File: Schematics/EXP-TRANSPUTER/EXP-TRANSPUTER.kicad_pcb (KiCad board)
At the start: 4 copper layers, 172 x 60 mm, 36 parts, among them IC2 74HCT373DW, IC5 CY62256N, J1 DIN41612_03x32_ABC_Male_Hor, J10 Conn_02x02_Odd_Even, J3 Conn_01x08, J4 Conn_01x08, J5 Conn_01x08, J6 Conn_01x08, J7 Conn_02x02_Odd_Even, J8 Conn_02x02_Odd_Even, J9 Conn_02x02_Odd_Even, U11 IMSC011, U2 ATF1502AS, U7 SN74LVC245APW

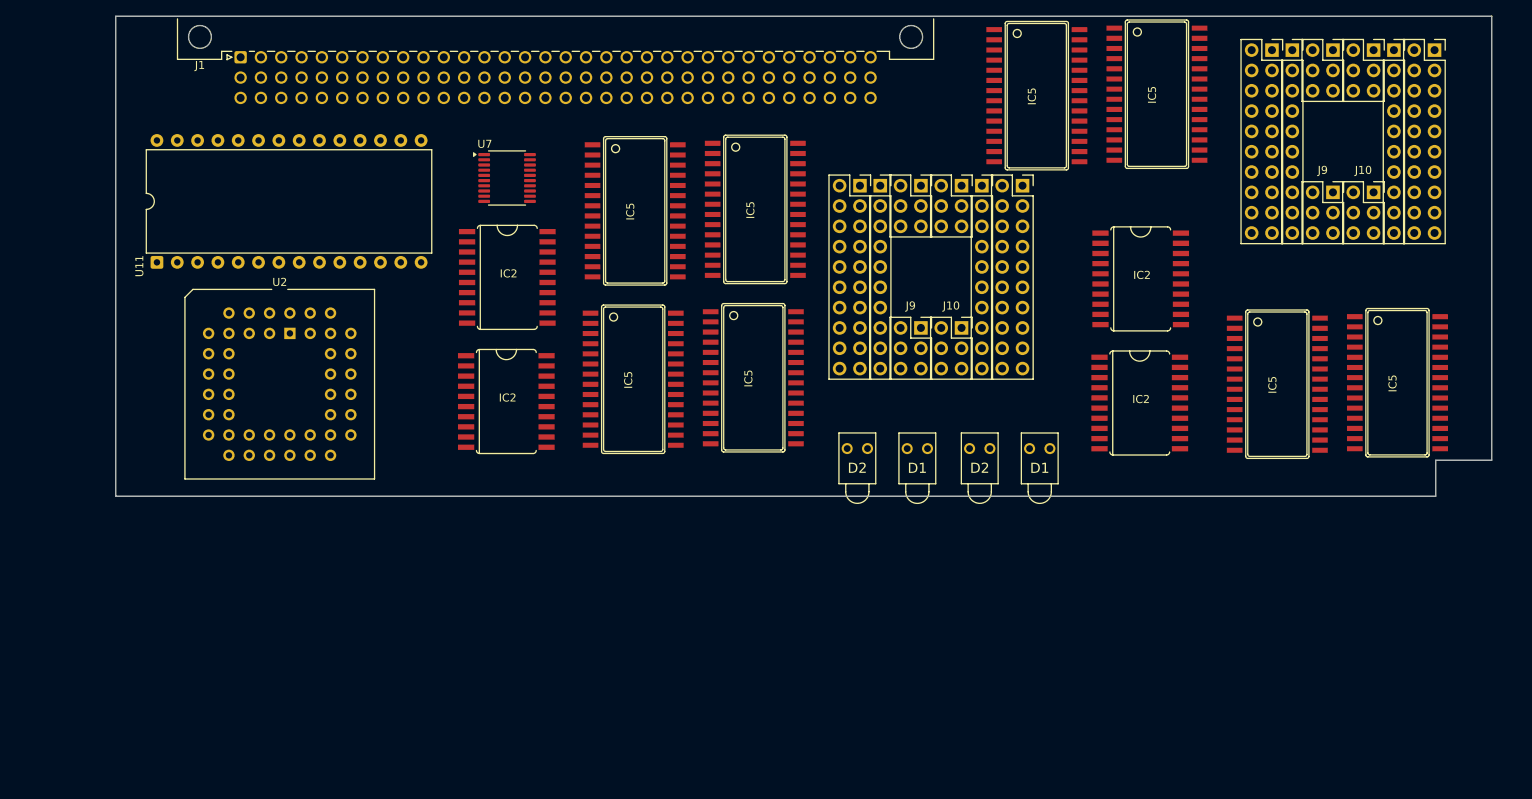
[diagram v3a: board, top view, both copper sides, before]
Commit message: Begun work on transputer expansion board
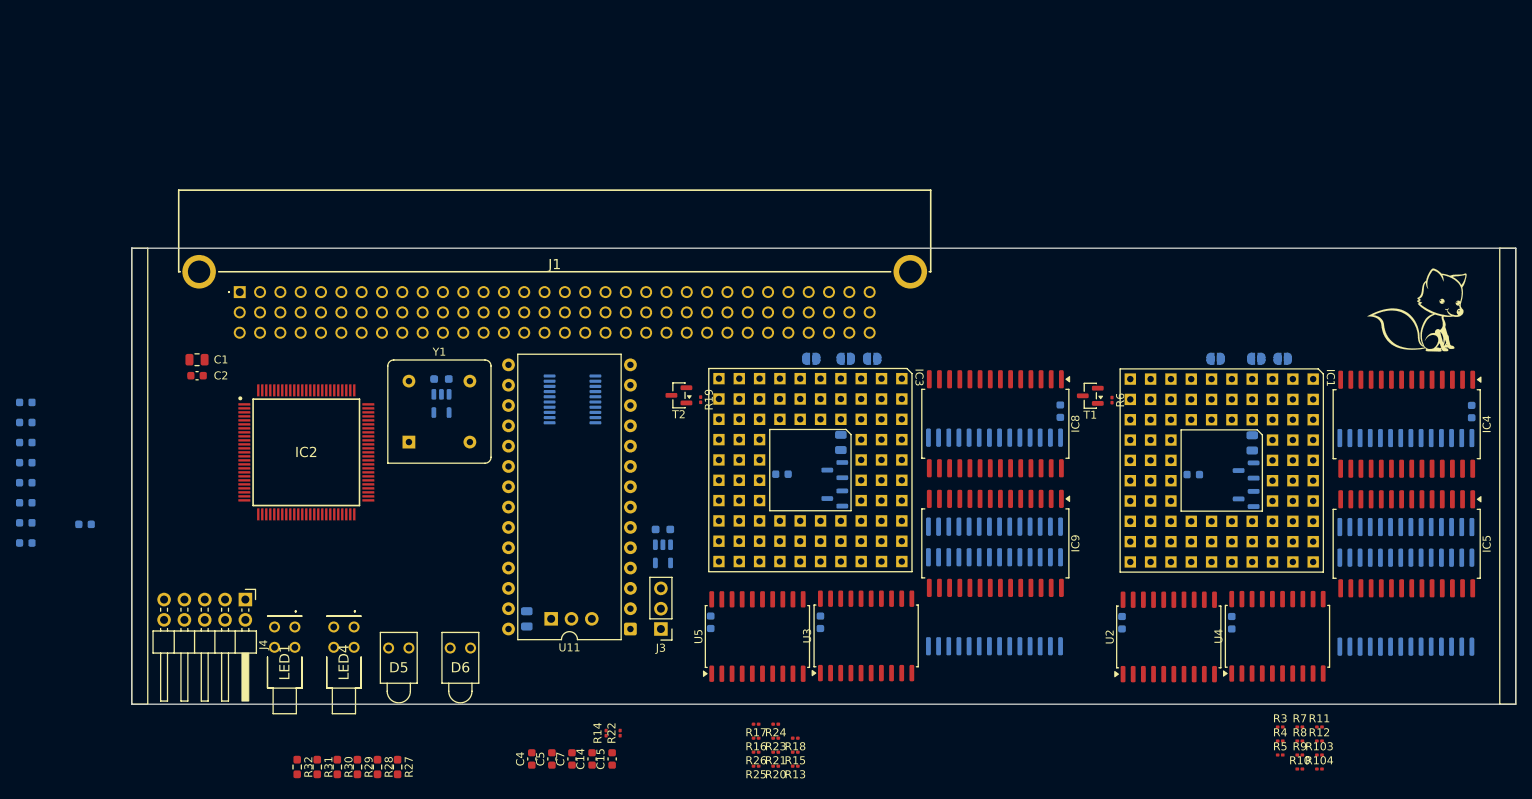
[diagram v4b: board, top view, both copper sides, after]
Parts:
- removed the D1 at (182.2, 95.0)
- removed the D1 at (166.9, 95.0)
- removed the D2 at (174.7, 95.0)
- removed the D2 at (159.4, 95.0)
- removed the IC2 at (116.9, 73.6)
- removed the IC2 at (116.8, 89.2)
- removed the IC2 at (196.0, 89.3)
- removed the IC2 at (196.1, 73.8)
- removed the IC5 at (183.1, 50.9)
- removed the IC5 at (132.9, 65.3)
- removed the IC5 at (198.2, 50.8)
- removed the IC5 at (147.7, 86.2)
- removed the IC5 at (213.2, 87.0)
- removed the IC5 at (228.2, 86.8)
- removed the IC5 at (147.9, 65.1)
- removed the IC5 at (132.7, 86.4)
- removed J10 (x2), J7 (x2), J8 (x2), J9 (x2): Conn_02x02_Odd_Even, Connector_PinSocket_2.54mm:PinSocket_2x03_P2.54mm_Vertical
- removed the J3 at (161.0, 62.2)
- removed the J3 at (212.5, 45.2)
- removed the J4 at (232.8, 45.2)
- removed the J4 at (181.3, 62.2)
- removed J5 (x2), J6 (x2): Conn_01x08, Connector_PinSocket_2.54mm:PinSocket_1x10_P2.54mm_Vertical
- added C1: 22uF 25V, Capacitor_SMD:C_0805_2012Metric, F.Cu at (78.2, 83.9)
- added C10: 100n, Capacitor_SMD:C_0603_1608Metric, B.Cu at (193.8, 116.8)
- added C11: 1u, Capacitor_SMD:C_0805_2012Metric, B.Cu at (210.1, 94.3)
- added C12: 100n, Capacitor_SMD:C_0603_1608Metric, B.Cu at (156.1, 116.8)
- added C13: 100n, Capacitor_SMD:C_0603_1608Metric, B.Cu at (186.1, 90.4)
- added C14: 100nF, Capacitor_SMD:C_0603_1608Metric, F.Cu at (127.5, 133.8)
- added C15: 100nF, Capacitor_SMD:C_0603_1608Metric, F.Cu at (130.0, 133.8)
- added C16: 100n, Capacitor_SMD:C_0603_1608Metric, B.Cu at (151.3, 98.2)
- added C17: 100n, Capacitor_SMD:C_0603_1608Metric, B.Cu at (142.4, 116.8)
- added C18: 1u, Capacitor_SMD:C_0805_2012Metric, B.Cu at (158.6, 94.3)
- added C19: 100nF, Capacitor_SMD:C_0603_1608Metric, B.Cu at (56.8, 89.3)
- added C2: 100nF, Capacitor_SMD:C_0603_1608Metric, F.Cu at (78.2, 85.9)
- added C20: 100nF, Capacitor_SMD:C_0603_1608Metric, B.Cu at (56.8, 91.8)
- added C21: 100nF, Capacitor_SMD:C_0603_1608Metric, B.Cu at (56.8, 94.3)
- added C22: 100nF, Capacitor_SMD:C_0603_1608Metric, B.Cu at (56.8, 96.8)
- added C23: 100nF, Capacitor_SMD:C_0603_1608Metric, B.Cu at (64.2, 104.5)
- added C24: 100nF, Capacitor_SMD:C_0603_1608Metric, B.Cu at (56.8, 99.3)
- added C25: 100nF, Capacitor_SMD:C_0603_1608Metric, B.Cu at (56.8, 101.8)
- added C26: 100nF, Capacitor_SMD:C_0603_1608Metric, B.Cu at (56.8, 104.3)
- added C27: 100nF, Capacitor_SMD:C_0603_1608Metric, B.Cu at (56.8, 106.8)
- added C3: 1uF 10V, Capacitor_SMD:C_0805_2012Metric, B.Cu at (119.4, 116.3)
- added C4: 100nF, Capacitor_SMD:C_0603_1608Metric, F.Cu at (120.0, 133.8)
- added C5: 100nF, Capacitor_SMD:C_0603_1608Metric, F.Cu at (122.5, 133.8)
- added C6: 100n, Capacitor_SMD:C_0603_1608Metric, B.Cu at (207.5, 116.8)
- added C7: 100nF, Capacitor_SMD:C_0603_1608Metric, F.Cu at (125.0, 133.8)
- added C8: 100n, Capacitor_SMD:C_0603_1608Metric, B.Cu at (237.5, 90.4)
- added C9: 100n, Capacitor_SMD:C_0603_1608Metric, B.Cu at (202.7, 98.3)
- added D1: BAV70, Package_TO_SOT_SMD:SOT-23, B.Cu at (209.3, 97.8)
- added D2: BAV70, Package_TO_SOT_SMD:SOT-23, B.Cu at (209.3, 101.3)
- added D3: BAV70, Package_TO_SOT_SMD:SOT-23, B.Cu at (157.9, 97.7)
- added D4: BAV70, Package_TO_SOT_SMD:SOT-23, B.Cu at (157.9, 101.3)
- added D5: LED, LTL-4221NHBP:LTL4221NHBP, F.Cu at (102.1, 120.0)
- added D6: LED, LTL-4221NHBP:LTL4221NHBP, F.Cu at (109.8, 120.0)
- added FOX1: SYM_Flash_Large, PaulasKiCADFootPrint:Fox_avatar_18mm, F.Cu at (231.4, 77.7)
- added IC1: IMST800, PaulasConnectors:PGA84, F.Cu at (217.7, 86.4)
- added IC10: CY62256N, Package_SO:SOP-28_8.4x18.16mm_P1.27mm, B.Cu at (177.8, 114.2)
- added IC11: CY62256N, Package_SO:SOP-28_8.4x18.16mm_P1.27mm, B.Cu at (177.8, 99.2)
- added IC2: ATF1508AS-7AX100, ATF1508ASL-nnAU100:QFP50P1600X1600X120-100N, F.Cu at (91.8, 95.5)
- added IC3: IMST800, PaulasConnectors:PGA84, F.Cu at (166.3, 86.3)
- added IC4: CY62256N, Package_SO:SOP-28_8.4x18.16mm_P1.27mm, F.Cu at (229.4, 92.0)
- added IC5: CY62256N, Package_SO:SOP-28_8.4x18.16mm_P1.27mm, F.Cu at (229.4, 107.0)
- added IC6: CY62256N, Package_SO:SOP-28_8.4x18.16mm_P1.27mm, B.Cu at (229.3, 114.2)
- added IC7: CY62256N, Package_SO:SOP-28_8.4x18.16mm_P1.27mm, B.Cu at (229.3, 99.3)
- added IC8: CY62256N, Package_SO:SOP-28_8.4x18.16mm_P1.27mm, F.Cu at (177.9, 91.9)
- added IC9: CY62256N, Package_SO:SOP-28_8.4x18.16mm_P1.27mm, F.Cu at (177.9, 106.9)
- added J2: Conn_01x03, Connector_PinHeader_2.54mm:PinHeader_1x03_P2.54mm_Horizontal, B.Cu at (122.4, 116.3)
- added J3: Conn_01x03, Connector_PinHeader_2.54mm:PinHeader_1x03_P2.54mm_Vertical, F.Cu at (136.1, 117.6)
- added J4: Conn_02x05_Odd_Even, Connector_PinHeader_2.54mm:PinHeader_2x05_P2.54mm_Horizontal, F.Cu at (84.2, 113.9)
- added JP10: Jumper_2_Open, Jumper:SolderJumper-2_P1.3mm_Open_RoundedPad1.0x1.5mm, B.Cu at (213.9, 83.8)
- added JP11: Jumper_2_Open, Jumper:SolderJumper-2_P1.3mm_Open_RoundedPad1.0x1.5mm, B.Cu at (205.5, 83.8)
- added JP12: Jumper_2_Open, Jumper:SolderJumper-2_P1.3mm_Open_RoundedPad1.0x1.5mm, B.Cu at (210.6, 83.8)
- added JP2: Jumper_2_Open, Jumper:SolderJumper-2_P1.3mm_Open_RoundedPad1.0x1.5mm, B.Cu at (162.6, 83.8)
- added JP4: Jumper_2_Open, Jumper:SolderJumper-2_P1.3mm_Open_RoundedPad1.0x1.5mm, B.Cu at (154.9, 83.8)
- added JP6: Jumper_2_Open, Jumper:SolderJumper-2_P1.3mm_Open_RoundedPad1.0x1.5mm, B.Cu at (159.3, 83.8)
- added LED1: LTL-42D1NMHDP1, LTL-42D1NMHDP1:LTL42D1NMHDP1, F.Cu at (90.4, 117.3)
- added LED4: LTL-42D1NMHDP1, LTL-42D1NMHDP1:LTL42D1NMHDP1, F.Cu at (97.8, 117.3)
- added R1: 10K, Resistor_SMD:R_0603_1608Metric_Pad0.98x0.95mm_HandSolder, B.Cu at (136.4, 105.2)
- added R10: 56, Resistor_SMD:R_0201_0603Metric, F.Cu at (216.0, 135.1)
- added R103: 10k, Resistor_SMD:R_0201_0603Metric, F.Cu at (218.5, 133.3)
- added R104: 10k, Resistor_SMD:R_0201_0603Metric, F.Cu at (218.5, 135.1)
- added R11: 56, Resistor_SMD:R_0201_0603Metric, F.Cu at (218.5, 129.8)
- added R12: 56, Resistor_SMD:R_0201_0603Metric, F.Cu at (218.5, 131.6)
- added R13: 10k, Resistor_SMD:R_0201_0603Metric, F.Cu at (152.9, 134.7)
- added R14: 10K, Resistor_SMD:R_0201_0603Metric, F.Cu at (129.3, 130.6)
- added R15: 10k, Resistor_SMD:R_0201_0603Metric, F.Cu at (152.9, 133.0)
- added R16: 10k, Resistor_SMD:R_0201_0603Metric, F.Cu at (148.0, 131.2)
- added R17: 10k, Resistor_SMD:R_0201_0603Metric, F.Cu at (148.0, 129.5)
- added R18: 10k, Resistor_SMD:R_0201_0603Metric, F.Cu at (152.9, 131.2)
- added R19: 10k, Resistor_SMD:R_0201_0603Metric, F.Cu at (141.1, 88.9)
- added R2: 10K, Resistor_SMD:R_0603_1608Metric_Pad0.98x0.95mm_HandSolder, B.Cu at (108.7, 86.4)
- added R20: 10k, Resistor_SMD:R_0201_0603Metric, F.Cu at (150.5, 134.7)
- added R21: 10k, Resistor_SMD:R_0201_0603Metric, F.Cu at (150.5, 133.0)
- added R22: 3K3, Resistor_SMD:R_0201_0603Metric, F.Cu at (131.0, 130.6)
- added R23: 56, Resistor_SMD:R_0201_0603Metric, F.Cu at (150.5, 131.2)
- added R24: 56, Resistor_SMD:R_0201_0603Metric, F.Cu at (150.5, 129.5)
- added R25: 56, Resistor_SMD:R_0201_0603Metric, F.Cu at (148.0, 134.7)
- added R26: 56, Resistor_SMD:R_0201_0603Metric, F.Cu at (148.0, 133.0)
- added R27: 470R, Resistor_SMD:R_0603_1608Metric_Pad0.98x0.95mm_HandSolder, F.Cu at (103.2, 134.9)
- added R28: 470R, Resistor_SMD:R_0603_1608Metric_Pad0.98x0.95mm_HandSolder, F.Cu at (100.7, 134.9)
- added R29: 470R, Resistor_SMD:R_0603_1608Metric_Pad0.98x0.95mm_HandSolder, F.Cu at (98.2, 134.9)
- added R3: 10k, Resistor_SMD:R_0201_0603Metric, F.Cu at (213.6, 129.8)
- added R30: 470R, Resistor_SMD:R_0603_1608Metric_Pad0.98x0.95mm_HandSolder, F.Cu at (95.7, 134.9)
- added R31: 470R, Resistor_SMD:R_0603_1608Metric_Pad0.98x0.95mm_HandSolder, F.Cu at (93.2, 134.9)
- added R32: 470R, Resistor_SMD:R_0603_1608Metric_Pad0.98x0.95mm_HandSolder, F.Cu at (90.7, 134.9)
- added R4: 10k, Resistor_SMD:R_0201_0603Metric, F.Cu at (213.6, 131.6)
- added R5: 10k, Resistor_SMD:R_0201_0603Metric, F.Cu at (213.6, 133.3)
- added R6: 10k, Resistor_SMD:R_0201_0603Metric, F.Cu at (192.5, 89.0)
- added R7: 10k, Resistor_SMD:R_0201_0603Metric, F.Cu at (216.0, 129.8)
- added R8: 10k, Resistor_SMD:R_0201_0603Metric, F.Cu at (216.0, 131.6)
- added R9: 56, Resistor_SMD:R_0201_0603Metric, F.Cu at (216.0, 133.3)
- added T1: BC847, Package_TO_SOT_SMD:SOT-23, F.Cu at (189.8, 88.4)
- added T2: BC847, Package_TO_SOT_SMD:SOT-23, F.Cu at (138.4, 88.4)
- added U1: SN74LVC1G125DBV, Package_TO_SOT_SMD:SOT-23-5, B.Cu at (136.4, 108.2)
- added U3: 74HC373, Package_SO:SOIC-20W_7.5x12.8mm_P1.27mm, F.Cu at (161.8, 118.5)
- added U4: 74HC373, Package_SO:SOIC-20W_7.5x12.8mm_P1.27mm, F.Cu at (213.2, 118.5)
- added U5: 74HC373, Package_SO:SOIC-20W_7.5x12.8mm_P1.27mm, F.Cu at (148.2, 118.5)
- added U6: SN74LVC1G125DBV, Package_TO_SOT_SMD:SOT-23-5, B.Cu at (108.7, 89.4)
- added Y1: CXO_DIP8, Oscillator:Oscillator_DIP-8, F.Cu at (104.6, 94.2)
- J1: value DIN41612_03x32_ABC_Male_Hor -> DIN41612_02x32_AC(CAPS); footprint Connector_DIN:DIN41612_C_3x32_Male_Horizontal_THT -> DIN41612_96_RA:86093967113745ELF
- U2: value ATF1502AS -> 74HC373; footprint Package_LCC:PLCC-44_THT-Socket -> Package_SO:SOIC-20W_7.5x12.8mm_P1.27mm
- U7: value SN74LVC245APW -> SN74LV245APW; moved to B.Cu
- moved U2 116.2 mm to (199.6, 118.6), turned to 90 degrees
- moved U11 74.9 mm to (132.3, 117.6), turned to 180 degrees
- moved J1 29.4 mm to (83.5, 75.5), turned to 180 degrees
- moved U7 28.9 mm to (125.1, 88.9), turned to 180 degrees
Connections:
- U11 pad 13: LA_RESET -> /LinkAdapter/LINKADAP_RESET
- U11 pad 17: /Link Adapter/SPEED_OUT -> /LinkAdapter/SPEED_OUT
- U11 pad 2: /Link Adapter/LINK_IN -> LA_LINK_IN
- U11 pad 25: LA_nCS -> /LinkAdapter/LINKADAP_nCS
- U11 pad 3: LA_RnW -> /LinkAdapter/LINKADAP_RnW
- U11 pad 5: /A0 -> /Connector/A0
- U11 pad 6: /A1 -> /Connector/A1
- U2 pad 1: RnW -> GND
- U2 pad 11: unconnected-(U2-I/O/PD1-Pad11) -> Net-(IC1-NOTMEMS1)
- U2 pad 12: /A5 -> /TRAMOnBoard/A14
- U2 pad 13: TMS -> /TRAMOnBoard/AD14
- U2 pad 14: /A6 -> /TRAMOnBoard/AD11
- U2 pad 15: +5V -> /TRAMOnBoard/A11
- U2 pad 16: /A7 -> /TRAMOnBoard/A4
- U2 pad 17: /A8 -> /TRAMOnBoard/AD4
- U2 pad 18: /A9 -> GND
- U2 pad 19: /A10 -> unconnected-(U2-O7-Pad19)
- U2 pad 2: SYSCLK -> /TRAMOnBoard/A12
- U2 pad 20: /A12 -> +5V
- U2 pad 3: +5V -> /TRAMOnBoard/AD12
- U2 pad 4: /A1 -> /TRAMOnBoard/AD13
- U2 pad 5: /A0 -> /TRAMOnBoard/A13
- U2 pad 6: /A2 -> /TRAMOnBoard/A15
- U2 pad 7: TDI -> /TRAMOnBoard/AD15
- U2 pad 8: nRES -> /TRAMOnBoard/AD16
- U2 pad 9: /A4 -> /TRAMOnBoard/A16
- U7 pad 1: LA_BUF_DIR -> /LinkAdapter/BUF_DIR
- U7 pad 19: LA_nCS -> /LinkAdapter/LINKADAP_nCS
- U7 pad 2: /Link Adapter/D0 -> /Connector/D0
- U7 pad 3: /Link Adapter/D1 -> /Connector/D1
- U7 pad 4: /Link Adapter/D2 -> /Connector/D2
- U7 pad 5: /Link Adapter/D3 -> /Connector/D3
- U7 pad 6: /Link Adapter/D4 -> /Connector/D4
- U7 pad 7: /Link Adapter/D5 -> /Connector/D5
- U7 pad 8: /Link Adapter/D6 -> /Connector/D6
- U7 pad 9: /Link Adapter/D7 -> /Connector/D7
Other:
- board size 172 x 60 mm -> 173 x 57 mm
- copper layers 4 -> 2
